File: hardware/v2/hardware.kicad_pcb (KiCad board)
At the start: 2 copper layers, 109.6 x 44.2 mm, 43 parts, among them J1 Screw_Terminal_1x03, J2 Screw_Terminal_01x02, J3 Screw_Terminal_1x03, J4 Barrel_Jack_Switch, J5 Screw_Terminal_01x02, J6 Screw_Terminal_01x02, J7 Screw_Terminal_01x02, P1 CONN_01X02, P2 CONN_01X08, Q0 2n7002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

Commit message: Added pressure sensor
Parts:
- R12, R13, R14, R15, R16, R17, R18: footprint Resistor_SMD:R_0805_2012Metric_Pad1.15x1.40mm_HandSolder -> Resistor_SMD:R_1206_3216Metric_Pad1.42x1.75mm_HandSolder
- U3: footprint Package_DIP:DIP-8_W8.89mm_SMDSocket_LongPads -> Package_SO:SOIC-8_3.9x4.9mm_P1.27mm
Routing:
- net +5V: track 109.6 -> 112.9 mm
- net Net-(R12-Pad1): track 8.02 -> 10.7 mm
- net GND: track 217.6 -> 220.2 mm
- net Net-(R12-Pad2): track 6.10 -> 8.11 mm
- removed copper zone on B.Cu, net GND
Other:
- board size 109.6 x 44.2 mm -> 91.4 x 44.4 mm

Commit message: V3 hardware
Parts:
- moved D3 4.76 mm to (207.6, 100.0)
- moved R15 2.23 mm to (146.2, 120.2)
- moved J4 2.10 mm to (209.4, 108.2)
- moved J2 1.80 mm to (202.1, 117.3)
- moved J6 1.80 mm to (183.4, 117.3)
- moved J5 1.80 mm to (201.9, 106.7)
- moved J7 1.80 mm to (183.4, 106.7)
- moved C1 1.80 mm to (202.0, 110.8)
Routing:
- net GND: track 220.2 -> 194.6 mm
- net Net-(D3-Pad2): track 17.0 -> 8.32 mm
- net +9V: track 47.3 -> 54.6 mm
- net Net-(J3-Pad3): track 35.7 -> 40.2 mm
- net +5V: track 112.9 -> 108.6 mm
- net Net-(R13-Pad2): track 14.7 -> 12.1 mm
- added copper zone on B.Cu, net GND
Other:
- board size 91.4 x 44.4 mm -> 89.2 x 43 mm

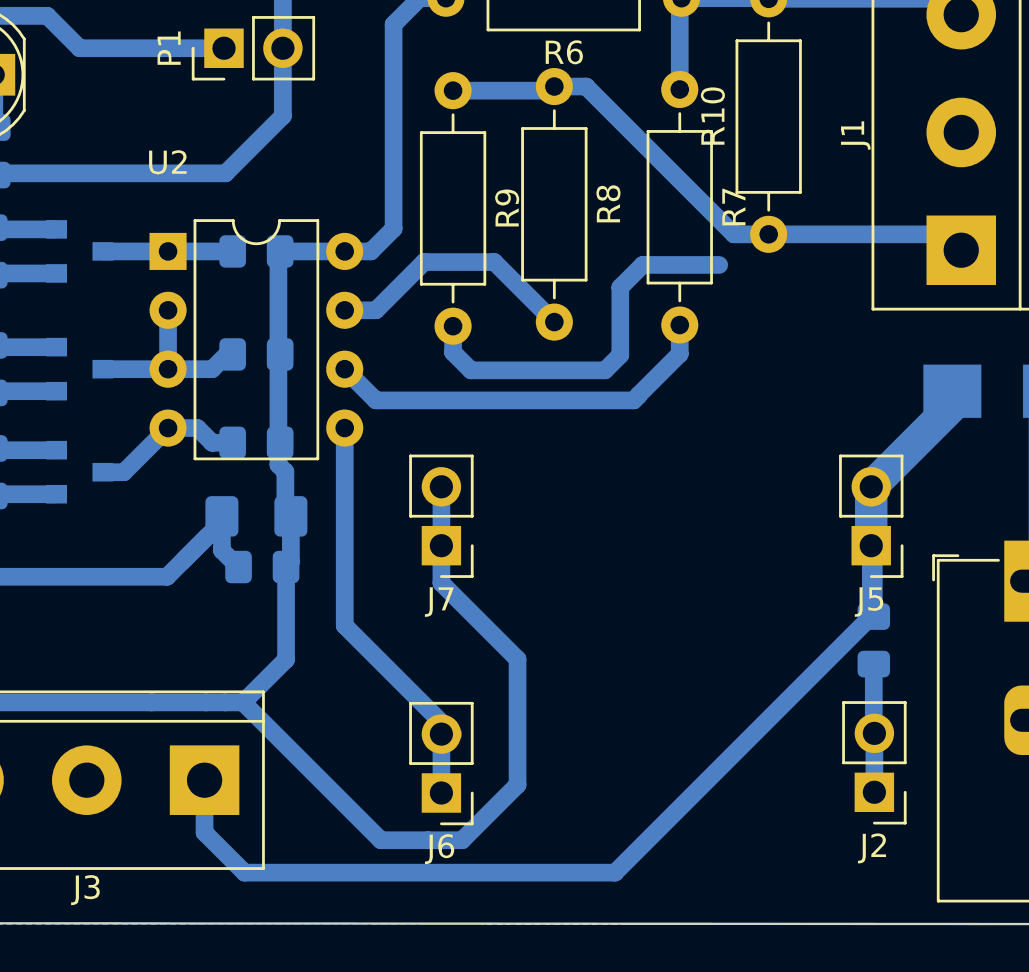
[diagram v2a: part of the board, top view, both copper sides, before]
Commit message: Corrected offset and display pressure in kgfm/cm2
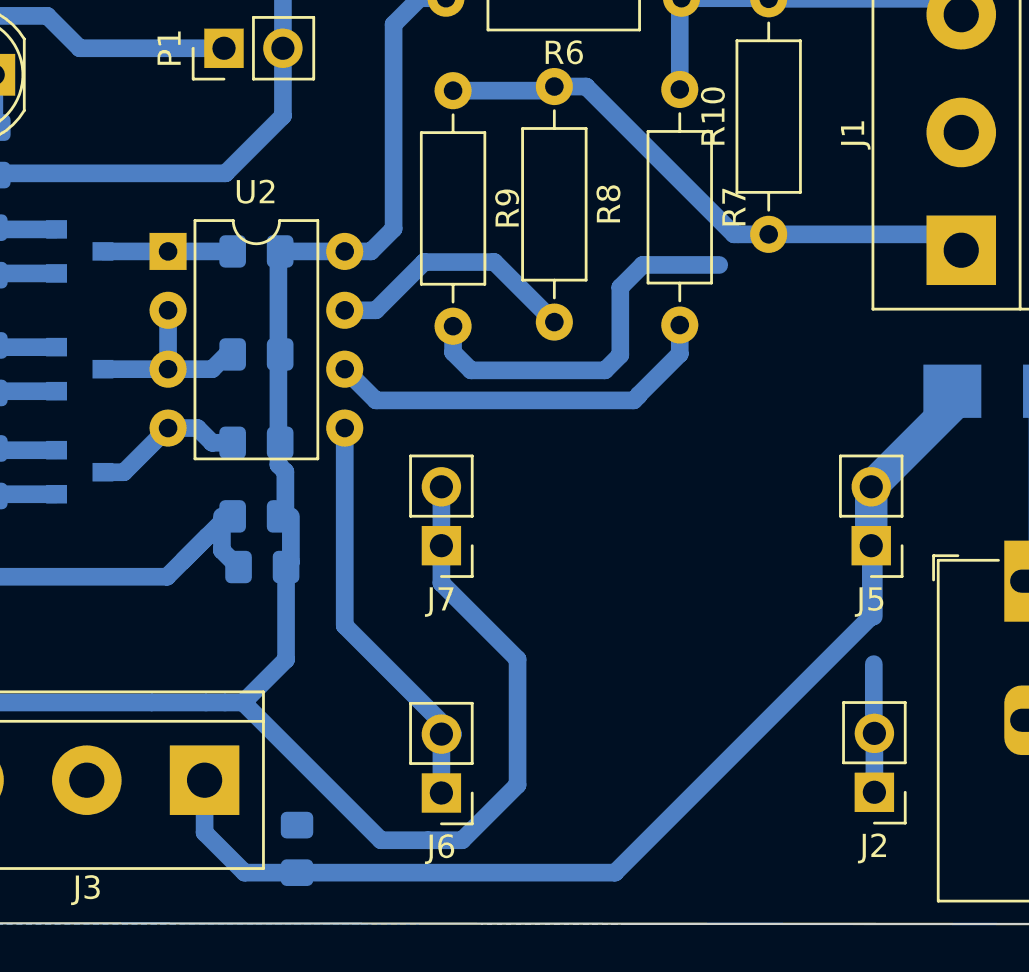
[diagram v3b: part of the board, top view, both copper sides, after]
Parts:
- C1: value 2.2u -> 100n
- C3: value 100n -> 2.2u; footprint Capacitor_SMD:C_1206_3216Metric_Pad1.42x1.75mm_HandSolder -> Capacitor_SMD:C_0805_2012Metric_Pad1.15x1.40mm_HandSolder
- R18: value 10k -> 0
- moved C1 26.5 mm to (177.2, 119.8), turned to 90 degrees
